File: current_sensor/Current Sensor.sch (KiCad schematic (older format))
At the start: 28 parts, among them P1 CAN_IN, P2 CAN_OUT, P3 DuraClik-5, P4 Ultra-Fit, P5 Ultra-Fit, P6 Ultra-Fit, Q1 Reverse, U1 ACS710, U2 NJM2870F0, U3 ACS710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

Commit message: moved the currrent sensor to a larger PCB
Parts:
- U1, U3, U5: footprint SMD_Packages:SO-16-W -> Supermileage:DIP-16-SchmartBoard
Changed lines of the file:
@@
 F 0 "U1" H 3400 3350 60  0000 C CNN
 F 1 "ACS710" H 3400 3450 60  0000 C CNN
-F 2 "SMD_Packages:SO-16-W" H 3300 3500 60  0001 C CNN
+F 2 "Supermileage:DIP-16-SchmartBoard" H 3300 3500 60  0001 C CNN
 F 3 "" H 3300 3500 60  0000 C CNN
 	1    3400 3550
@@
 F 0 "U3" H 6350 3350 60  0000 C CNN
 F 1 "ACS710" H 6350 3450 60  0000 C CNN
-F 2 "SMD_Packages:SO-16-W" H 6250 3500 60  0001 C CNN
+F 2 "Supermileage:DIP-16-SchmartBoard" H 6250 3500 60  0001 C CNN
 F 3 "" H 6250 3500 60  0000 C CNN
 	1    6350 3550
@@
 F 0 "U5" H 9250 3350 60  0000 C CNN
 F 1 "ACS710" H 9250 3450 60  0000 C CNN
-F 2 "SMD_Packages:SO-16-W" H 9150 3500 60  0001 C CNN
+F 2 "Supermileage:DIP-16-SchmartBoard" H 9150 3500 60  0001 C CNN
 F 3 "" H 9150 3500 60  0000 C CNN
 	1    9250 3550

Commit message: added more silkscreen text
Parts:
- P1, P2: PN 538-53261-0471 -> 538-502352-0400
- P3: Distributor (none) -> Mouser; PN (none) -> 538-502352-0501
- P4, P5, P6: Distributor (none) -> Mouser; PN (none) -> 538-172310-2102
- Q1: Distributor (none) -> Mouser; PN (none) -> 863-NTR3A30PZT1G
- U2: Distributor (none) -> Mouser; PN (none) -> 513-NJM2870F05-TE2
- U4: Distributor (none) -> Mouser; PN (none) -> 998-MIC5317-3.3YM5TR
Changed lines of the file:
@@
 F 2 "Supermileage:Molex-UltraFit-2p" H 2500 3550 50  0001 C CNN
 F 3 "" H 2500 3550 50  0000 C CNN
+F 4 "Mouser" H 2500 3550 60  0001 C CNN "Distributor"
+F 5 "538-172310-2102 " H 2500 3550 60  0001 C CNN "PN"
 	1    2500 3550
 	-1   0    0    -1
@@
 F 2 "User_Connectors:Molex-duraClick-5conn" H 1150 1250 50  0001 C CNN
 F 3 "" H 1150 1250 50  0000 C CNN
+F 4 "Mouser" H 1150 1250 60  0001 C CNN "Distributor"
+F 5 "538-502352-0501 " H 1150 1250 60  0001 C CNN "PN"
 	1    1150 1250
 	-1   0    0    1
@@
 F 2 "TO_SOT_Packages_SMD:SOT-23-5" H 5100 1100 60  0001 C CNN
 F 3 "" H 5100 1100 60  0000 C CNN
+F 4 "Mouser" H 5100 1150 60  0001 C CNN "Distributor"
+F 5 "513-NJM2870F05-TE2 " H 5100 1150 60  0001 C CNN "PN"
 	1    5100 1150
 	1    0    0    -1
@@
 F 2 "TO_SOT_Packages_SMD:SOT-23_Handsoldering" H 4350 1350 50  0001 C CNN
 F 3 "" H 4150 1250 50  0000 C CNN
+F 4 "Mouser" H 4150 1250 60  0001 C CNN "Distributor"
+F 5 "863-NTR3A30PZT1G " H 4150 1250 60  0001 C CNN "PN"
 	1    4150 1250
 	0    -1   -1   0
@@
 F 2 "Supermileage:Molex-UltraFit-2p" H 5450 3550 50  0001 C CNN
 F 3 "" H 5450 3550 50  0000 C CNN
+F 4 "Mouser" H 5450 3550 60  0001 C CNN "Distributor"
+F 5 "538-172310-2102 " H 5450 3550 60  0001 C CNN "PN"
 	1    5450 3550
 	-1   0    0    -1
@@
 F 2 "Supermileage:Molex-UltraFit-2p" H 8350 3550 50  0001 C CNN
 F 3 "" H 8350 3550 50  0000 C CNN
+F 4 "Mouser" H 8350 3550 60  0001 C CNN "Distributor"
+F 5 "538-172310-2102 " H 8350 3550 60  0001 C CNN "PN"
 	1    8350 3550
 	-1   0    0    -1
@@
 F 2 "TO_SOT_Packages_SMD:SOT-23-5" H 7450 1200 60  0001 C CNN
 F 3 "" H 7450 1200 60  0000 C CNN
+F 4 "Mouser" H 7450 1250 60  0001 C CNN "Distributor"
+F 5 "998-MIC5317-3.3YM5TR " H 7450 1250 60  0001 C CNN "PN"
 	1    7450 1250
 	1    0    0    -1
@@
 F 3 "" H 1100 3250 50  0000 C CNN
 F 4 "Mouser" H 1100 3250 60  0001 C CNN "Distributor"
-F 5 "538-53261-0471" H 1100 3250 60  0001 C CNN "PN"
+F 5 "538-502352-0400 " H 1100 3250 60  0001 C CNN "PN"
 	1    1100 3250
 	-1   0    0    1
@@
 F 3 "" H 1100 2650 50  0000 C CNN
 F 4 "Mouser" H 1100 2650 60  0001 C CNN "Distributor"
-F 5 "538-53261-0471" H 1100 2650 60  0001 C CNN "PN"
+F 5 "538-502352-0400 " H 1100 2650 60  0001 C CNN "PN"
 	1    1100 2650
 	-1   0    0    1

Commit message: fixed some stuff
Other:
- note added: "Analog outputs directly from the current sensors"
- note added: "PMOS as an ideal diode. \nWhen the gate goes below Vgs the transistor turns on."
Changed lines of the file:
@@
 Text Label 1450 1050 0    60   ~ 0
 Vin
+Text Notes 725  800  0    60   ~ 0
+Analog outputs directly from the current sensors
+Text Notes 3525 825  0    60   ~ 0
+PMOS as an ideal diode. \nWhen the gate goes below Vgs the transistor turns on.
 $EndSCHEMATC

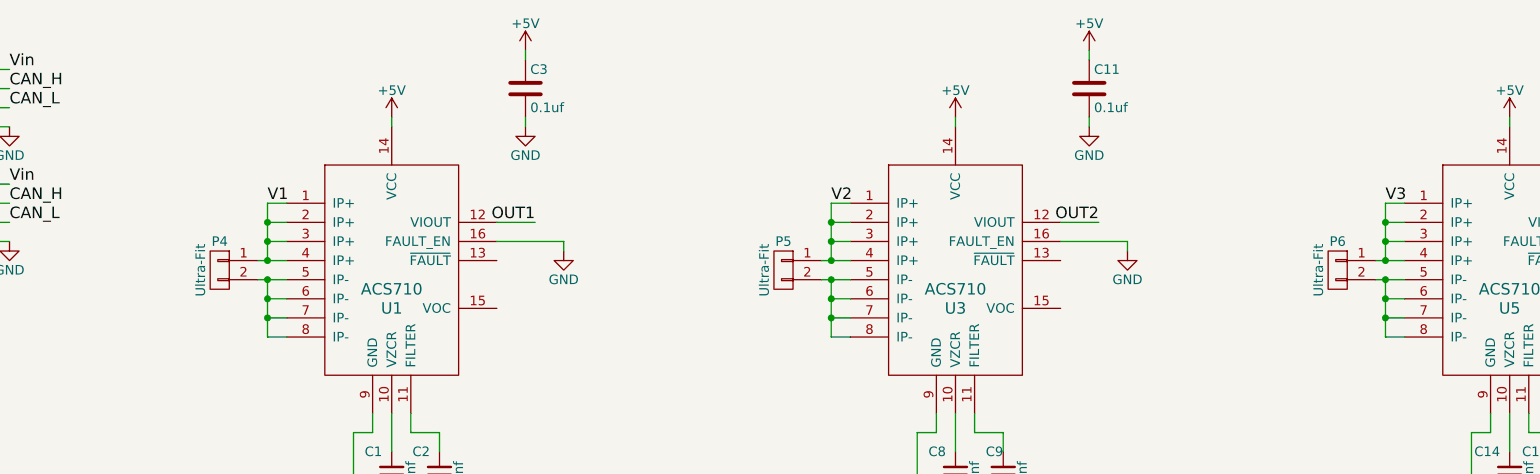
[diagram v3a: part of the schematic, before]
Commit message: Moved to four pin Molex UltraFit connectors.
Required rearanging layout slightly.
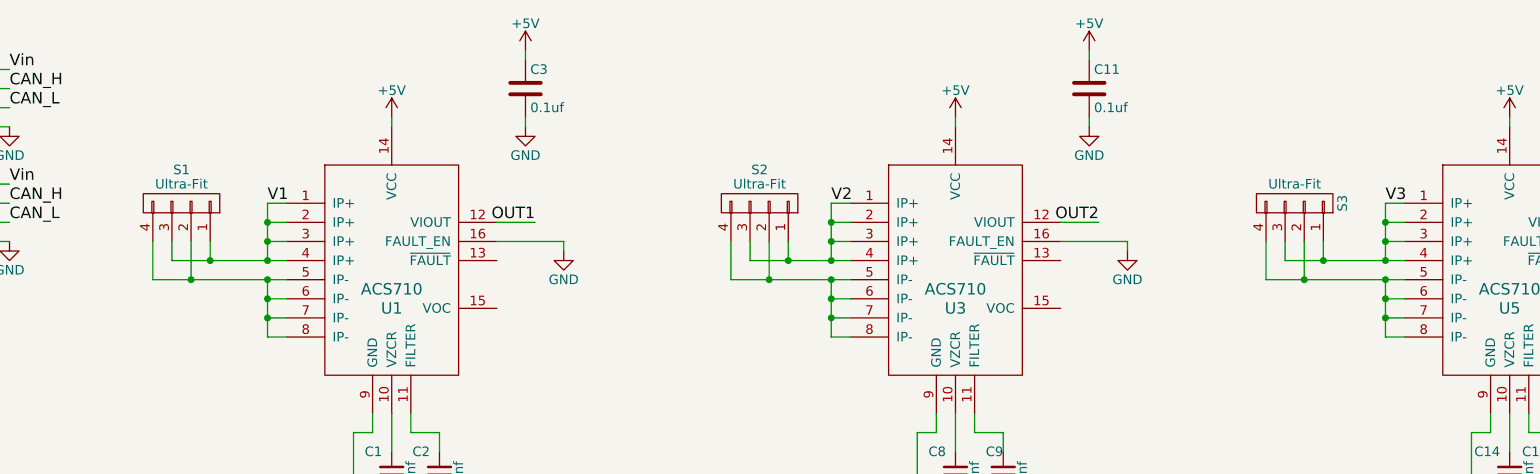
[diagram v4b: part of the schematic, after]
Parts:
- removed P4, P5, P6: Ultra-Fit, Supermileage:Molex-UltraFit-2p, symbol CONN_01X02
- added S1, S2, S3: Ultra-Fit, supermileage_footprints:Molex-UltraFit-4p, symbol CONN_01X04
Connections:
- net V1: now also S1.1 (P1), S1.3 (P3)
- net V2: now also S2.1 (P1), S2.3 (P3)
- net V3: now also S3.1 (P1), S3.3 (P3)
- net at U1.5 (IP-), U1.6 (IP-), U1.7 (IP-)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: now also S1.2 (P2), S1.4 (P4)
- net at U3.5 (IP-), U3.6 (IP-), U3.7 (IP-)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: now also S2.2 (P2), S2.4 (P4)
- net at U5.5 (IP-), U5.6 (IP-), U5.7 (IP-)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: now also S3.2 (P2), S3.4 (P4)
